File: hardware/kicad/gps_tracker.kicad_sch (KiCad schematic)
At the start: 13 parts, among them J1 GNSS: Foxeer M10Q-250 / Beiti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, J2 BIGGA GSM (SIM800C) board, J3 SSD1306 0.96" OLED I2C 0x3C, J4 MicroSD SPI module, J5 Battery Shield V8, 2x18650, J6 BMA400 CJMCU-400, SW1 Button (BOOT-style, active lo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, U1 ESP32-S3-WROOM-1 (DevKitC-1)

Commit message: C1 1000 µF at the modem in every drawing; sequence diagrams for the three main flows
The 1000 µF electrolytic across the BIGGA board's VSS and GND pins ended
the resets on battery (hardware/README.md §5, README results), but the
component table, the power tree, the schematic, the wiring diagram and
the assembly sheet still said "no external capacitor". All five now carry
C1: a Device:C_Polarized on the +5V net next to J2 in the schematic (ERC
still 0/0), an electrolytic symbol across the modem's supply wires in the
wiring diagram, a row in the module table and a word in the assembly step.

docs/ARCHITECTURE.md §2 gains three Mermaid sequence diagrams: a fix
becoming a record on the card and a point on the map (popped from the
uplink queue only after HTTP 200), an upload failing three different ways
(no answer, server rejection, modem-side error) with the three different
answers, and the park / sleep / wake cycle. The README shows the first
and links the others. GitHub renders Mermaid inline.
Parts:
- added C1: 1000u, symbol Device:C_Polarized
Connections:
- net +5V: now also C1.1
- net GND: now also C1.2
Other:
- note added: "Silkscreen: GND TX (5 V level!) -> IO18 RX <- IO17 PK = BOOT/PWRKEY <- IO7 (open drain) VSS = VCC 5V in NET 6 NET -> R4 1k -> LED1 (NETLIGHT: 0.8 s searching, 3 s registered, 0.3 s GPRS) 7 DTR 8 RING 9-12 audio: unused. TX high side is pulled to VCC through 4.7k on the board: R3 divides it to ~3.0 V for IO18. VBAT is 3.64 V (MIC29302). C1 1000 uF across VSS/GND right at the board's pins (+ to VSS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"
- note removed: "Silkscreen: GND TX (5 V level!) -> IO18 RX <- IO17 PK = BOOT/PWRKEY <- IO7 (open drain) VSS = VCC 5V in NET 6 NET -> R4 1k -> LED1 (NETLIGHT: 0.8 s searching, 3 s registered, 0.3 s GPRS) 7 DTR 8 RING 9-12 audio: unused. TX high side is pulled to VCC through 4.7k on the board: R3 divides it to ~3.0 V for IO18. VBAT is 3.64 V (MIC29302), 100+10+1 uF already on VCC: short thick wires keep VCC above 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"

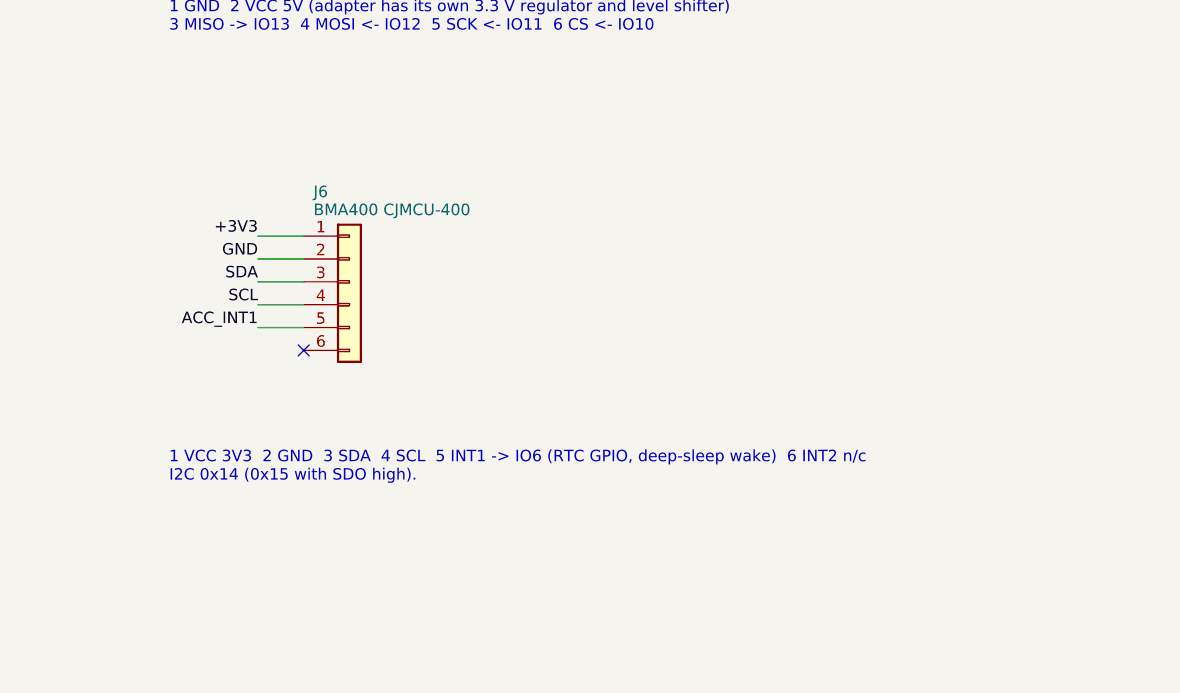
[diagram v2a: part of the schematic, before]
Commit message: Wiring diagram: wider modules, subtitles that fit, BMA400 CS and SDO ties drawn
The module boxes were 200 px wide and several subtitles and notes ran past
their borders. The canvas grows to 1320 x 840, the module columns to
250 px, the devkit and the channels shift with them, and a subtitle may
wrap onto a second line (the MicroSD and BMA400 boxes). Every text now
sits inside its box.

The accelerometer's CS pin tied to 3.3 V, which fixed the chip starting
in SPI mode on one power-up in three, had not reached the drawings: the
wiring diagram, the schematic (J6 is now an 8-pin header, ERC 0/0) and the
assembly sheet show CS to 3V3 and SDO to GND (optional, fixes the address
at 0x14). The hardware notes' component table names both ties.
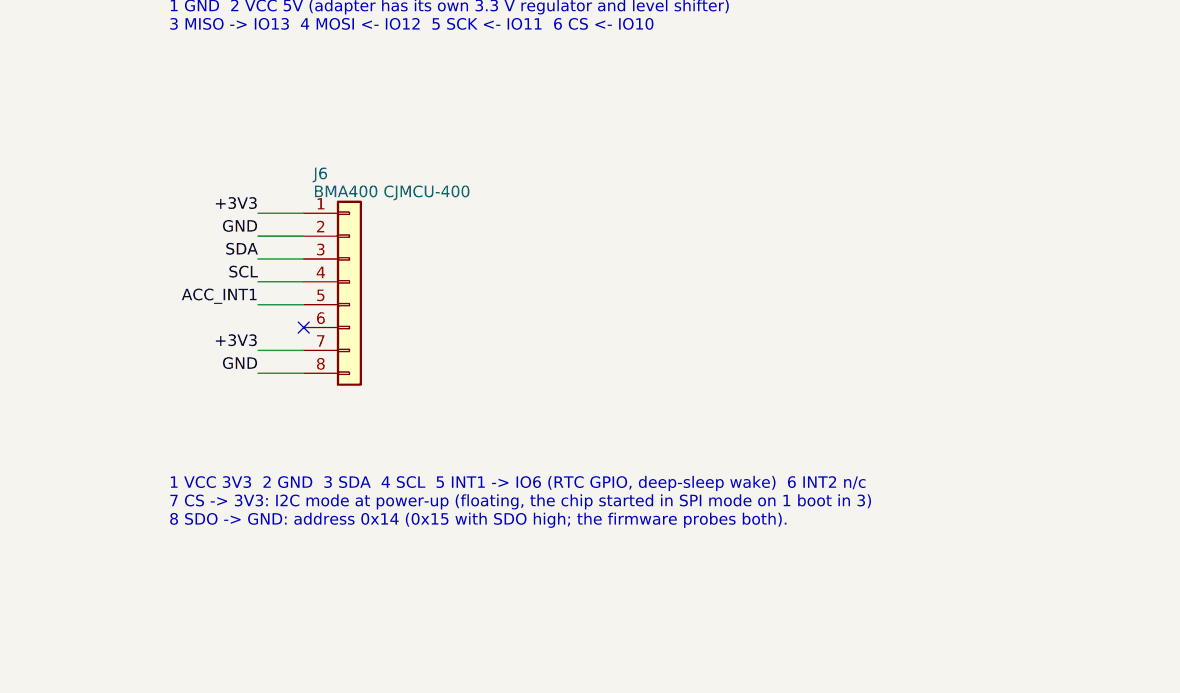
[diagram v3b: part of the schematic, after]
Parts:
- removed J6: BMA400 CJMCU-400, symbol Connector_Generic:Conn_01x06
- added J6: BMA400 CJMCU-400, symbol Connector_Generic:Conn_01x08
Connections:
- net +3V3: now also J6.1 (Pin_1), J6.7 (Pin_7)
- net ACC_INT1: now also J6.5 (Pin_5)
- net GND: now also J6.2 (Pin_2), J6.8 (Pin_8)
- net SCL: now also J6.4 (Pin_4)
- net SDA: now also J6.3 (Pin_3)
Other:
- note added: "1 VCC 3V3 2 GND 3 SDA 4 SCL 5 INT1 -> IO6 (RTC GPIO, deep-sleep wake) 6 INT2 n/c 7 CS -> 3V3: I2C mode at power-up (floating, the chip started in SPI mode on 1 boot in 3) 8 SDO -> GND: address 0x14 (0x15 with SDO high; the firmware probes both)."
- note removed: "1 VCC 3V3 2 GND 3 SDA 4 SCL 5 INT1 -> IO6 (RTC GPIO, deep-sleep wake) 6 INT2 n/c I2C 0x14 (0x15 with SDO high)."

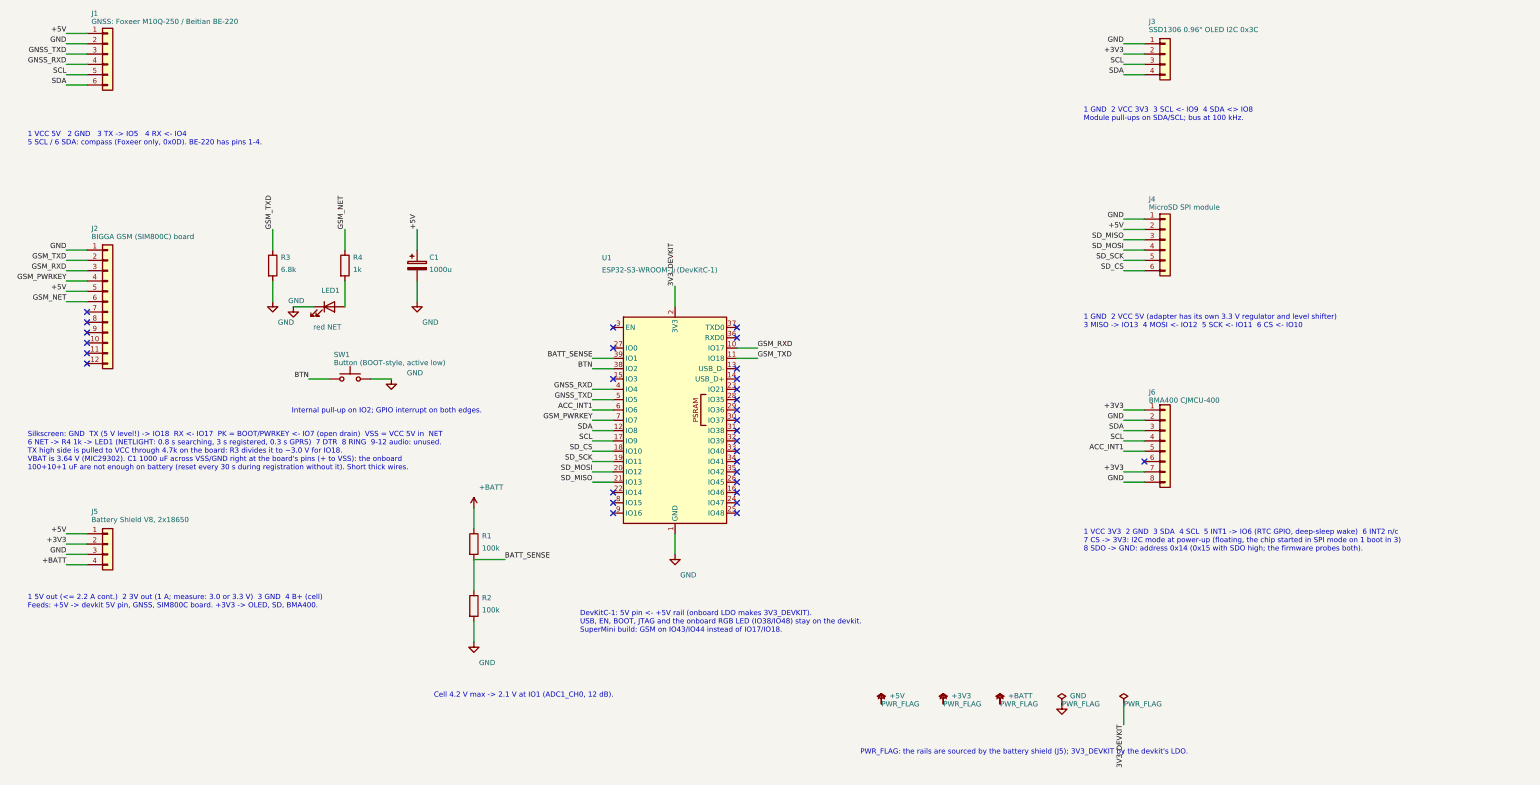
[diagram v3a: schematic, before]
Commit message: Drawings and documents for the SuperMini build: PWRKEY RC filter, 3-pin button module
Wiring diagram (tools/gen_wiring_svg.py, hardware/wiring.svg): the
SuperMini in the middle with the modem UART on GPIO43/44, R5 1k and C2
100n in the PWRKEY wire, the 3-pin button module on 3V3/GND/GPIO2, and
notes for the board's 5V pin (USB VBUS, shield only with USB unplugged)
and the DevKitC's GPIO17/18.

KiCad schematic (tools/gen_schematic.py, hardware/kicad/): U1 is the
SuperMini on TXD0/RXD0, PWRKEY_GPIO -> R5 -> GSM_PWRKEY with C2 to GND,
J7 the button module in place of SW1, 3V3_BOARD for the board's LDO.
ERC clean; PDF and SVG re-exported.

Assembly sheet: the new diagram embedded, warnings for the 5V pin and the
PWRKEY filter, the pin map, module tables and checklist for the
SuperMini (USB Serial/JTAG console, -e supermini).

READMEs: SuperMini as the default build; results for the button wiring,
the attach resets and how they were isolated (DevKitC radiated pickup,
SuperMini PWRKEY wire, RC fix) and the cold-start date; the DevKitC's
radio sensitivity under known issues; component table with R5/C2 and
the button module; resolved open questions ticked. Changelog entry for
the unreleased changes.
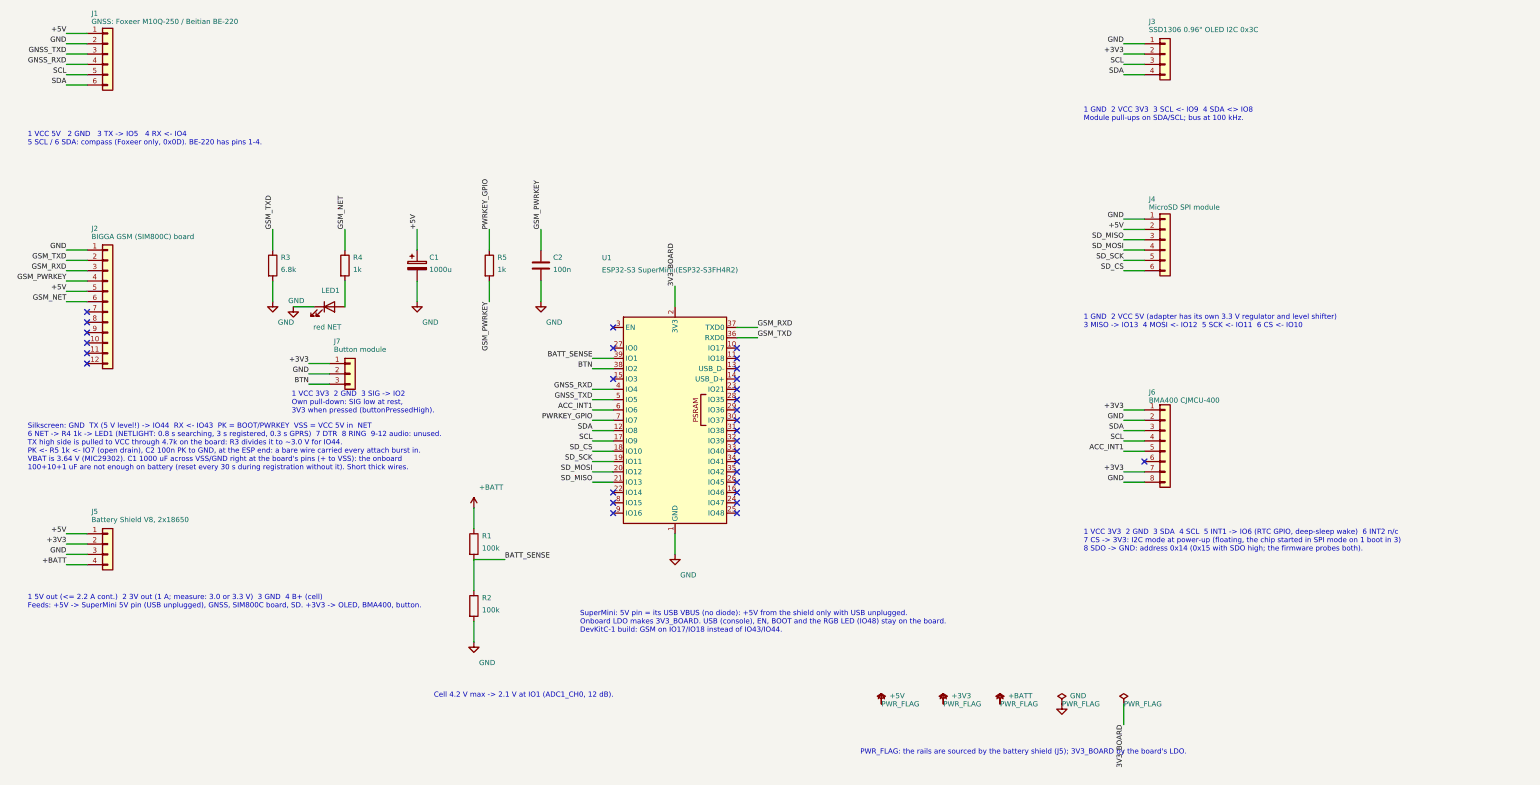
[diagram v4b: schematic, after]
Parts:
- removed SW1: Button (BOOT-style, active low), symbol Switch:SW_Push
- added C2: 100n, symbol Device:C
- added J7: Button module, symbol Connector_Generic:Conn_01x03
- added R5: 1k, symbol Device:R
- U1: value ESP32-S3-WROOM-1 (DevKitC-1) -> ESP32-S3 SuperMini (ESP32-S3FH4R2)
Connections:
- net +3V3: now also J7.1 (Pin_1)
- net BTN: now also J7.3 (Pin_3)
- net GND: now also C2.2, J7.2 (Pin_2)
- net GSM_PWRKEY: now also C2.1, R5.2; no longer U1.7 (IO7)
- net GSM_RXD: now also U1.37 (TXD0); no longer U1.10 (IO17)
- net GSM_TXD: now also U1.36 (RXD0); no longer U1.11 (IO18)
- net 3V3_DEVKIT renamed 3V3_BOARD
- new net PWRKEY_GPIO: R5.1, U1.7 (IO7)
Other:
- note added: "1 5V out (<= 2.2 A cont.) 2 3V out (1 A; measure: 3.0 or 3.3 V) 3 GND 4 B+ (cell) Feeds: +5V -> SuperMini 5V pin (USB unplugged), GNSS, SIM800C board, SD. +3V3 -> OLED, BMA400, button."
- note added: "1 VCC 3V3 2 GND 3 SIG -> IO2 Own pull-down: SIG low at rest, 3V3 when pressed (buttonPressedHigh)."
- note added: "PWR_FLAG: the rails are sourced by the battery shield (J5); 3V3_BOARD by the board's LDO."
- note added: "Silkscreen: GND TX (5 V level!) -> IO44 RX <- IO43 PK = BOOT/PWRKEY VSS = VCC 5V in NET 6 NET -> R4 1k -> LED1 (NETLIGHT: 0.8 s searching, 3 s registered, 0.3 s GPRS) 7 DTR 8 RING 9-12 audio: unused. TX high side is pulled to VCC through 4.7k on the board: R3 divides it to ~3.0 V for IO44. PK <- R5 1k <- IO7 (open drain), C2 100n PK to GND, at the ESP end: a bare wire carried every attach burst i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"
- note added: "SuperMini: 5V pin = its USB VBUS (no diode): +5V from the shield only with USB unplugged. Onboard LDO makes 3V3_BOARD. USB (console), EN, BOOT and the RGB LED (IO48) stay on the board. DevKitC-1 build: GSM on IO17/IO18 instead of IO43/IO44."
- note removed: "1 5V out (<= 2.2 A cont.) 2 3V out (1 A; measure: 3.0 or 3.3 V) 3 GND 4 B+ (cell) Feeds: +5V -> devkit 5V pin, GNSS, SIM800C board. +3V3 -> OLED, SD, BMA400."
- note removed: "DevKitC-1: 5V pin <- +5V rail (onboard LDO makes 3V3_DEVKIT). USB, EN, BOOT, JTAG and the onboard RGB LED (IO38/IO48) stay on the devkit. SuperMini build: GSM on IO43/IO44 instead of IO17/IO18."
- note removed: "Internal pull-up on IO2; GPIO interrupt on both edges."
- note removed: "PWR_FLAG: the rails are sourced by the battery shield (J5); 3V3_DEVKIT by the devkit's LDO."
- note removed: "Silkscreen: GND TX (5 V level!) -> IO18 RX <- IO17 PK = BOOT/PWRKEY <- IO7 (open drain) VSS = VCC 5V in NET 6 NET -> R4 1k -> LED1 (NETLIGHT: 0.8 s searching, 3 s registered, 0.3 s GPRS) 7 DTR 8 RING 9-12 audio: unused. TX high side is pulled to VCC through 4.7k on the board: R3 divides it to ~3.0 V for IO18. VBAT is 3.64 V (MIC29302). C1 1000 uF across VSS/GND right at the board's pins (+ to VSS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"
